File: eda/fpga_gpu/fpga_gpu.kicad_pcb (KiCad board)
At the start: 2 copper layers, 94.5 x 72.4 mm, 70 parts, among them J1 VGA, J2 Bus expansion, J3 programming, J4 reset ground, Q1 2N7002, SW1 SW_Reset, SW2 SW_FlashPwrCycle, U1 ICE40HX4K-TQ144, U10 IS61C5128AL-10KLI, U2 SST25VF080B-50-4x-S2Ax, U3 74HCT541, U4 74HCT541, U5 74HCT541, U6 TXS0108EPW, U7 TXS0108EPW, U8 AMS1117-3.3, U9 AP2112K-1.2, X1 TXC-7C

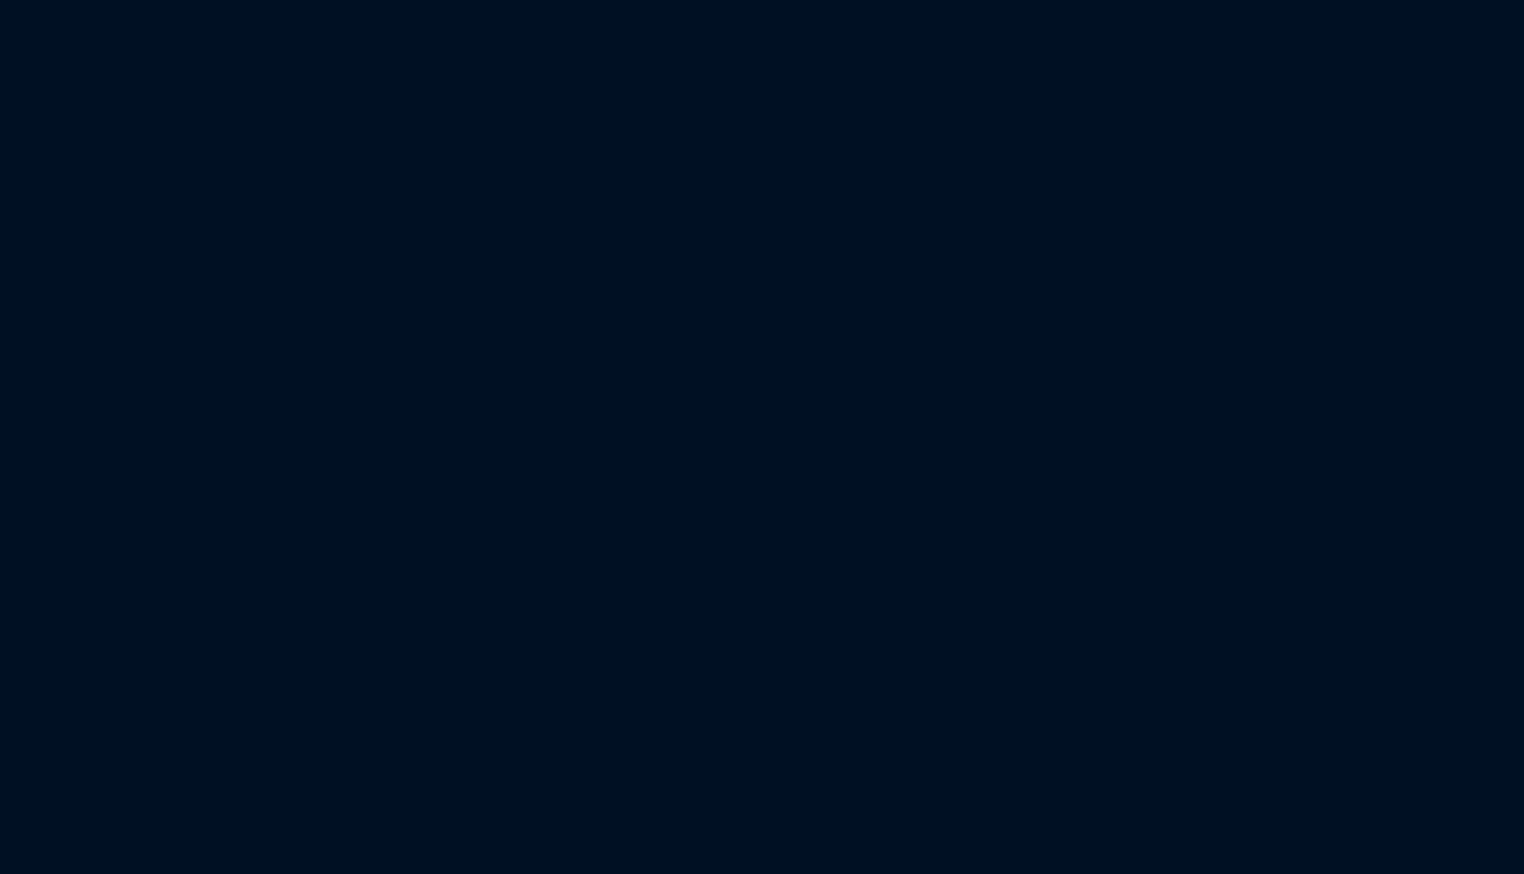
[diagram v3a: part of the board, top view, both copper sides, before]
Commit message: Add skeleton stuff to io-card and gpu
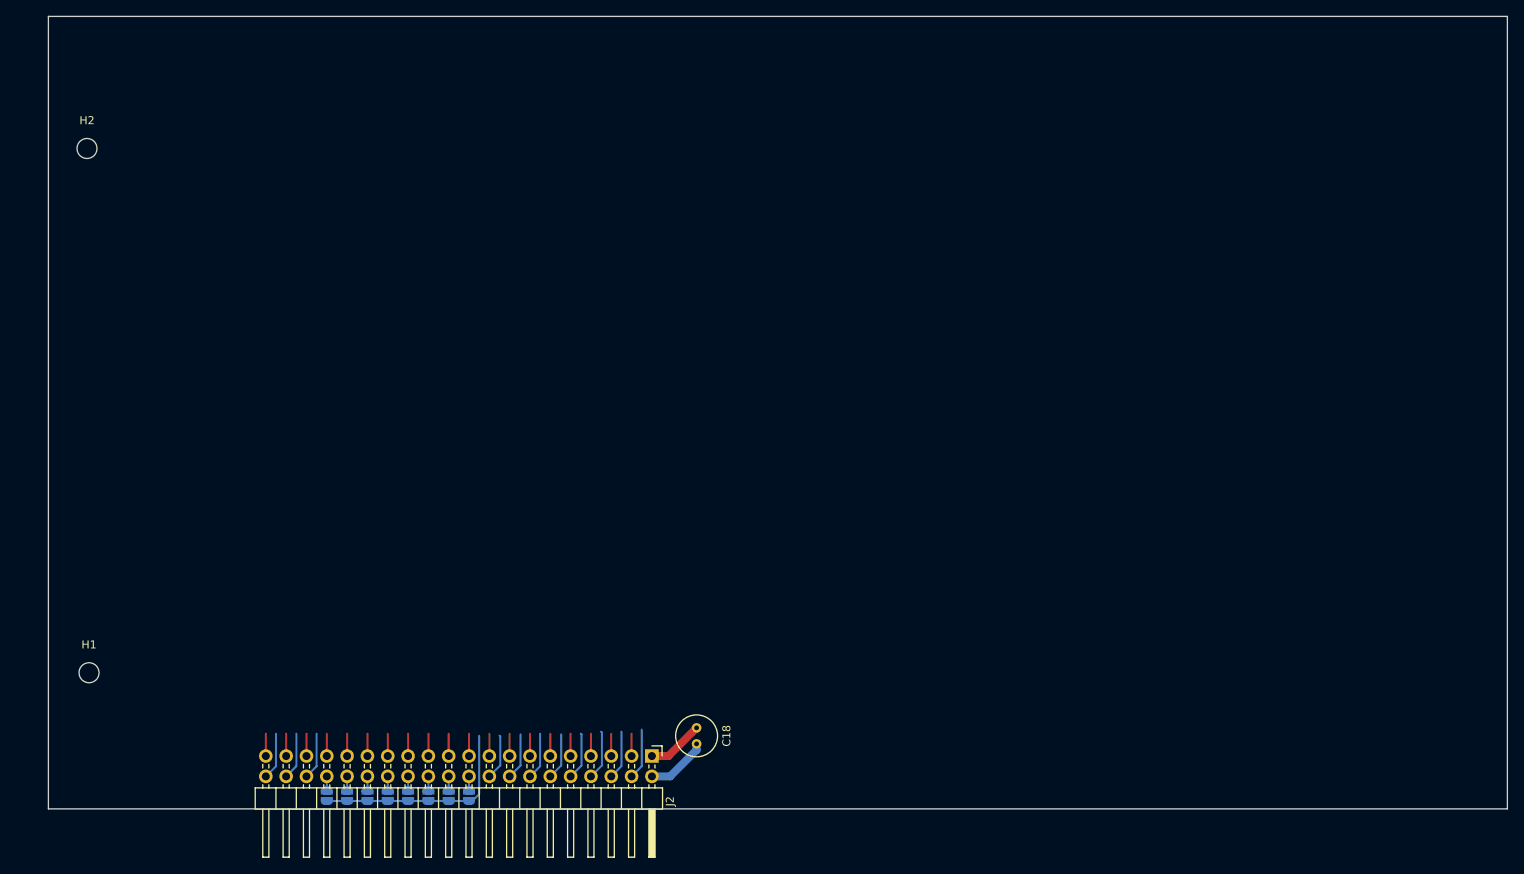
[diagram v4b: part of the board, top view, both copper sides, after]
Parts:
- added C18: 100nf, Capacitor_THT:C_Radial_D5.0mm_H7.0mm_P2.00mm, F.Cu at (400.9, 123.2)
- added H1: Bracket mounting, MountingHole:MountingHole_2.5mm, F.Cu at (325.0, 116.3)
- added H2: Bracket mounting, MountingHole:MountingHole_2.5mm, F.Cu at (324.7, 50.8)
- added J2: Bus expansion, Connector_PinHeader_2.54mm:PinHeader_2x20_P2.54mm_Horizontal, F.Cu at (395.3, 126.7)
- added JP1: SolderJumper_2_Open, Jumper:SolderJumper-2_P1.3mm_Open_RoundedPad1.0x1.5mm, B.Cu at (372.5, 131.7)
- added JP2: SolderJumper_2_Open, Jumper:SolderJumper-2_P1.3mm_Open_RoundedPad1.0x1.5mm, B.Cu at (369.9, 131.7)
- added JP3: SolderJumper_2_Open, Jumper:SolderJumper-2_P1.3mm_Open_RoundedPad1.0x1.5mm, B.Cu at (367.4, 131.7)
- added JP4: SolderJumper_2_Open, Jumper:SolderJumper-2_P1.3mm_Open_RoundedPad1.0x1.5mm, B.Cu at (364.8, 131.7)
- added JP5: SolderJumper_2_Open, Jumper:SolderJumper-2_P1.3mm_Open_RoundedPad1.0x1.5mm, B.Cu at (362.3, 131.7)
- added JP6: SolderJumper_2_Open, Jumper:SolderJumper-2_P1.3mm_Open_RoundedPad1.0x1.5mm, B.Cu at (359.8, 131.7)
- added JP7: SolderJumper_2_Open, Jumper:SolderJumper-2_P1.3mm_Open_RoundedPad1.0x1.5mm, B.Cu at (357.2, 131.7)
- added JP8: SolderJumper_2_Open, Jumper:SolderJumper-2_P1.3mm_Open_RoundedPad1.0x1.5mm, B.Cu at (354.7, 131.7)
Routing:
- net (no net): track 1.17 -> 161.1 mm
- net Net-(J2-Pin_34): track 0.00 -> 1.78 mm
- net Net-(J2-Pin_32): track 0.00 -> 1.78 mm
- net Net-(J2-Pin_30): track 0.00 -> 1.78 mm
- net Net-(J2-Pin_28): track 0.00 -> 1.78 mm
- net Net-(J2-Pin_26): track 0.00 -> 1.78 mm
- net Net-(J2-Pin_24): track 0.00 -> 1.78 mm
- net Net-(J2-Pin_22): track 0.00 -> 1.78 mm
- net Net-(J2-Pin_20): track 0.00 -> 1.78 mm
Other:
- board size 94.5 x 72.4 mm -> 482.4 x 99.1 mm
- board text added: "0"
- board text added: "1"
- board text added: "2"
- board text added: "3"
- board text added: "4"
- board text added: "5"
- board text added: "6"
- board text added: "7"

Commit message: Add expansion backplane
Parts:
- removed the C18 at (29.0, 52.6)
- removed the H1 at (111.0, 49.5)
- removed the H2 at (23.1, 49.5)
- removed H3, H4: MountingHole, MountingHole:MountingHole_2.5mm
- removed the J2 at (24.9, 59.9)
- removed the JP1 at (31.1, 82.8)
- removed the JP2 at (31.1, 85.3)
- removed the JP3 at (31.1, 87.9)
- removed the JP4 at (31.1, 90.4)
- removed the JP5 at (31.1, 93.0)
- removed the JP6 at (31.1, 95.5)
- removed the JP7 at (31.1, 98.0)
- removed the JP8 at (31.1, 100.6)
- added C24: 100n, Capacitor_SMD:C_0805_2012Metric, F.Cu at (66.2, 139.0)
- added U11: 74HCT00, Package_SO:SSOP-14_5.3x6.2mm_P0.65mm, F.Cu at (71.0, 138.9)
- H1, H2: value Bracket mounting -> MountingHole
- moved H2 270.5 mm to (56.1, 82.8)
- moved H1 269.3 mm to (56.4, 135.4)
- moved J2 269.3 mm to (126.7, 145.8)
- moved JP1 269.3 mm to (103.9, 150.8)
- moved JP3 269.3 mm to (98.8, 150.8)
- moved JP5 269.3 mm to (93.7, 150.8)
- moved JP6 269.3 mm to (91.2, 150.8)
- moved JP8 269.3 mm to (86.1, 150.8)
- moved C18 269.3 mm to (132.3, 142.3)
- moved JP2 269.3 mm to (101.3, 150.8)
- moved JP4 269.3 mm to (96.3, 150.8)
- moved JP7 269.3 mm to (88.6, 150.8)
- moved C22 121.5 mm to (128.6, 133.3), turned to 0 degrees
- moved C20 121.1 mm to (124.8, 133.3), turned to 180 degrees
- moved U8 112.5 mm to (124.8, 127.3), turned to 90 degrees
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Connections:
- C18 pad 1: (no net) -> VCC
- C18 pad 2: (no net) -> GND
- J2 pad 1: (no net) -> VCC
- J2 pad 10: (no net) -> /Interfacing/Expansion/D3
- J2 pad 11: (no net) -> /Interfacing/Expansion/A4
- J2 pad 12: (no net) -> /Interfacing/Expansion/D4
- J2 pad 13: (no net) -> /Interfacing/Expansion/A5
- J2 pad 14: (no net) -> /Interfacing/Expansion/D5
- J2 pad 15: (no net) -> /Interfacing/Expansion/A6
- J2 pad 16: (no net) -> /Interfacing/Expansion/D6
- J2 pad 17: (no net) -> /Interfacing/Expansion/A7
- J2 pad 18: (no net) -> /Interfacing/Expansion/D7
- J2 pad 19: (no net) -> /Interfacing/Expansion/A8
- J2 pad 2: (no net) -> GND
- J2 pad 21: (no net) -> /Interfacing/Expansion/A9
- J2 pad 23: (no net) -> /Interfacing/Expansion/A10
- J2 pad 25: (no net) -> /Interfacing/Expansion/A11
- J2 pad 27: (no net) -> /Interfacing/Expansion/A12
- J2 pad 29: (no net) -> /Interfacing/Expansion/A13
- J2 pad 3: (no net) -> /Interfacing/Expansion/A0
- J2 pad 31: (no net) -> /Interfacing/Expansion/A14
- J2 pad 33: (no net) -> /Interfacing/Expansion/A15
- J2 pad 35: (no net) -> /Interfacing/Clock-VCC
- J2 pad 36: (no net) -> /Interfacing/Expansion/~{RST}
- J2 pad 37: (no net) -> /Interfacing/R~{W}-VCC
- J2 pad 38: (no net) -> /Interfacing/Expansion/~{NMI}
- J2 pad 39: (no net) -> /Interfacing/Expansion/~{DMA}
- J2 pad 4: (no net) -> /Interfacing/Expansion/D0
- J2 pad 40: (no net) -> /Interfacing/~{IRQ}
- J2 pad 5: (no net) -> /Interfacing/Expansion/A1
- J2 pad 6: (no net) -> /Interfacing/Expansion/D1
- J2 pad 7: (no net) -> /Interfacing/Expansion/A2
- J2 pad 8: (no net) -> /Interfacing/Expansion/D2
- J2 pad 9: (no net) -> /Interfacing/Expansion/A3
- JP1 pad 2: (no net) -> /Interfacing/~{CS}-VCC
- JP2 pad 2: (no net) -> /Interfacing/~{CS}-VCC
- JP3 pad 2: (no net) -> /Interfacing/~{CS}-VCC
- JP4 pad 2: (no net) -> /Interfacing/~{CS}-VCC
- JP5 pad 2: (no net) -> /Interfacing/~{CS}-VCC
- JP6 pad 2: (no net) -> /Interfacing/~{CS}-VCC
- JP7 pad 2: (no net) -> /Interfacing/~{CS}-VCC
- JP8 pad 2: (no net) -> /Interfacing/~{CS}-VCC
- U1 pad 110: /Interfacing/ADev3 -> unconnected-(U1A-IOT_168-Pad110)
- U1 pad 112: /Interfacing/ADev2 -> /Interfacing/R~{W}
- U1 pad 113: /Interfacing/ADev1 -> /Interfacing/~{RST}
- U1 pad 114: /Interfacing/ADev0 -> /Interfacing/~{CS}
- U1 pad 115: /Interfacing/Clock -> /Interfacing/ADev3
- U1 pad 116: /Interfacing/~{CS} -> /Interfacing/ADev2
- U1 pad 117: /Interfacing/R~{W} -> /Interfacing/ADev1
- U1 pad 118: /Interfacing/~{RST} -> /Interfacing/ADev0
- U1 pad 128: /FpgaIRQ -> unconnected-(U1A-IOT_197_GBIN1-Pad128)
- U1 pad 129: unconnected-(U1A-IOT_198_GBIN0-Pad129) -> /Interfacing/Clock
- U1 pad 28: unconnected-(U1D-IOL_23A-Pad28) -> /~{RamWE}
- U1 pad 43: /~{RamCE} -> unconnected-(U1C-IOB_71-Pad43)
- U1 pad 44: /~{RamWE} -> unconnected-(U1C-IOB_72-Pad44)
- U1 pad 45: /~{RamOE} -> unconnected-(U1C-IOB_73-Pad45)
- U1 pad 48: unconnected-(U1C-IOB_80-Pad48) -> /RamIo3
- U1 pad 49: unconnected-(U1C-IOB_81_GBIN5-Pad49) -> /RamIo2
- U1 pad 52: /RamIo7 -> /RamIo4
- U1 pad 55: /RamIo6 -> /RamIo5
- U1 pad 56: /RamIo5 -> /RamIo1
- U1 pad 60: /RamIo4 -> /RamIo6
- U1 pad 62: /RamIo1 -> /RamIo7
- U1 pad 63: /RamIo2 -> /~{RamCE}
- U1 pad 64: /RamIo3 -> /~{RamOE}
- U1 pad 74: unconnected-(U1B-IOR_110-Pad74) -> /FpgaIRQ
- U3 pad 2: /Interfacing/Expansion/A3 -> /Interfacing/Clock-VCC
- U3 pad 3: /Interfacing/Expansion/A2 -> /Interfacing/R~{W}-VCC
- U3 pad 4: /Interfacing/Expansion/A1 -> /Interfacing/Expansion/~{RST}
- U3 pad 5: /Interfacing/Expansion/A0 -> /Interfacing/~{CS}-VCC
- U3 pad 6: /Interfacing/Expansion/Clock -> /Interfacing/Expansion/A3
- U3 pad 7: /Interfacing/Expansion/~{CS} -> /Interfacing/Expansion/A2
- U3 pad 8: /Interfacing/Expansion/R~{W} -> /Interfacing/Expansion/A1
- U3 pad 9: /Interfacing/Expansion/~{RST} -> /Interfacing/Expansion/A0
- U4 pad 2: /Interfacing/Expansion/D0 -> /Interfacing/Expansion/D7
- U4 pad 3: /Interfacing/Expansion/D1 -> /Interfacing/Expansion/D6
- U4 pad 4: /Interfacing/Expansion/D2 -> /Interfacing/Expansion/D5
- U4 pad 5: /Interfacing/Expansion/D3 -> /Interfacing/Expansion/D4
- U4 pad 6: /Interfacing/Expansion/D4 -> /Interfacing/Expansion/D3
- U4 pad 7: /Interfacing/Expansion/D5 -> /Interfacing/Expansion/D2
- U4 pad 8: /Interfacing/Expansion/D6 -> /Interfacing/Expansion/D1
- U4 pad 9: /Interfacing/Expansion/D7 -> /Interfacing/Expansion/D0
- U5 pad 1: unconnected-(U5-G1-Pad1) -> Net-(U5-G1)
- U5 pad 11: /Interfacing/Expansion/D0 -> /Interfacing/Expansion/D7
- U5 pad 12: /Interfacing/Expansion/D1 -> /Interfacing/Expansion/D6
- U5 pad 13: /Interfacing/Expansion/D2 -> /Interfacing/Expansion/D5
- U5 pad 14: /Interfacing/Expansion/D3 -> /Interfacing/Expansion/D4
- U5 pad 15: /Interfacing/Expansion/D4 -> /Interfacing/Expansion/D3
- U5 pad 16: /Interfacing/Expansion/D5 -> /Interfacing/Expansion/D2
- U5 pad 17: /Interfacing/Expansion/D6 -> /Interfacing/Expansion/D1
- U5 pad 18: /Interfacing/Expansion/D7 -> /Interfacing/Expansion/D0
- U5 pad 19: unconnected-(U5-G2-Pad19) -> /Interfacing/~{CS}-VCC
- U5 pad 2: /DOut7 -> /DOut0
- U5 pad 3: /DOut6 -> /DOut1
- U5 pad 4: /DOut5 -> /DOut2
- U5 pad 5: /DOut4 -> /DOut3
- U5 pad 6: /DOut3 -> /DOut4
- U5 pad 7: /DOut2 -> /DOut5
- U5 pad 8: /DOut1 -> /DOut6
- U5 pad 9: /DOut0 -> /DOut7
- U6 pad 12: /DIn7 -> /DIn0
- U6 pad 13: /DIn6 -> /DIn1
- U6 pad 14: /DIn5 -> /DIn2
- U6 pad 15: /DIn4 -> /DIn3
- U6 pad 16: /DIn3 -> /DIn4
- U6 pad 17: /DIn2 -> /DIn5
- U6 pad 18: /DIn1 -> /DIn6
- U6 pad 20: /DIn0 -> /DIn7
- U7 pad 12: /Interfacing/~{RST} -> /Interfacing/ADev0
- U7 pad 13: /Interfacing/R~{W} -> /Interfacing/ADev1
- U7 pad 14: /Interfacing/~{CS} -> /Interfacing/ADev2
- U7 pad 15: /Interfacing/Clock -> /Interfacing/ADev3
- U7 pad 16: /Interfacing/ADev0 -> /Interfacing/~{CS}
- U7 pad 17: /Interfacing/ADev1 -> /Interfacing/~{RST}
- U7 pad 18: /Interfacing/ADev2 -> /Interfacing/R~{W}
- U7 pad 20: /Interfacing/ADev3 -> /Interfacing/Clock
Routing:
- net (no net): track 161.1 -> 1.17 mm
- net /FpgaIRQ: track 39.8 -> 107.4 mm
- net VCC: track 278.1 -> 224.3 mm, vias 10 -> 9
- net /Interfacing/~{CS}-VCC: track 0.00 -> 50.7 mm, vias 0 -> 1
- net GND: track 235.2 -> 188.1 mm, vias 47 -> 53
- net Net-(U5-G1): track 0.00 -> 46.8 mm, vias 0 -> 2
- net /RamA9: track 58.5 -> 13.4 mm
- net /Interfacing/R~{W}-VCC: track 0.00 -> 42.9 mm, vias 0 -> 1
- net /RamA8: track 56.4 -> 13.8 mm
- net /Interfacing/Expansion/D0: track 20.5 -> 61.5 mm
- net /~{RamOE}: track 12.6 -> 53.1 mm
- net /Interfacing/Clock-VCC: track 0.00 -> 39.9 mm, vias 0 -> 1
- net /RamA7: track 53.5 -> 14.1 mm
- net /Interfacing/Expansion/D1: track 21.2 -> 60.2 mm
- net unconnected-(J1-Pad0): track 37.2 -> 0.00 mm
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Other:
- board size 482.4 x 99.1 mm -> 99.3 x 75.9 mm
- board text added: "Dedicated to Emil, who loves the trace"
- board text added: "IO0"
- board text added: "IO1"
- board text added: "IO2"
- board text added: "IO3"
- board text added: "IO4"
- board text added: "IO5"
- board text added: "IO6"
- board text added: "IO7"

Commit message: Interim commit
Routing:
- net GND: track 188.1 -> 186.2 mm
- net VCC: track 224.3 -> 223.6 mm
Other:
- board text added: "Dedicated to Emil, who loves this trace"
- board text removed: "Dedicated to Emil, who loves the trace"
